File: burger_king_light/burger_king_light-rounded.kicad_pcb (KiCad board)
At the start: 2 copper layers, 102.1 x 58.7 mm, 58 parts, among them U1 TPS55340PWPR, U2 ICM7555CBAZ, U3 IS32LT3178-GRLA3-TR, U4 IS32LT3178-GRLA3-TR, U5 IS32LT3178-GRLA3-TR

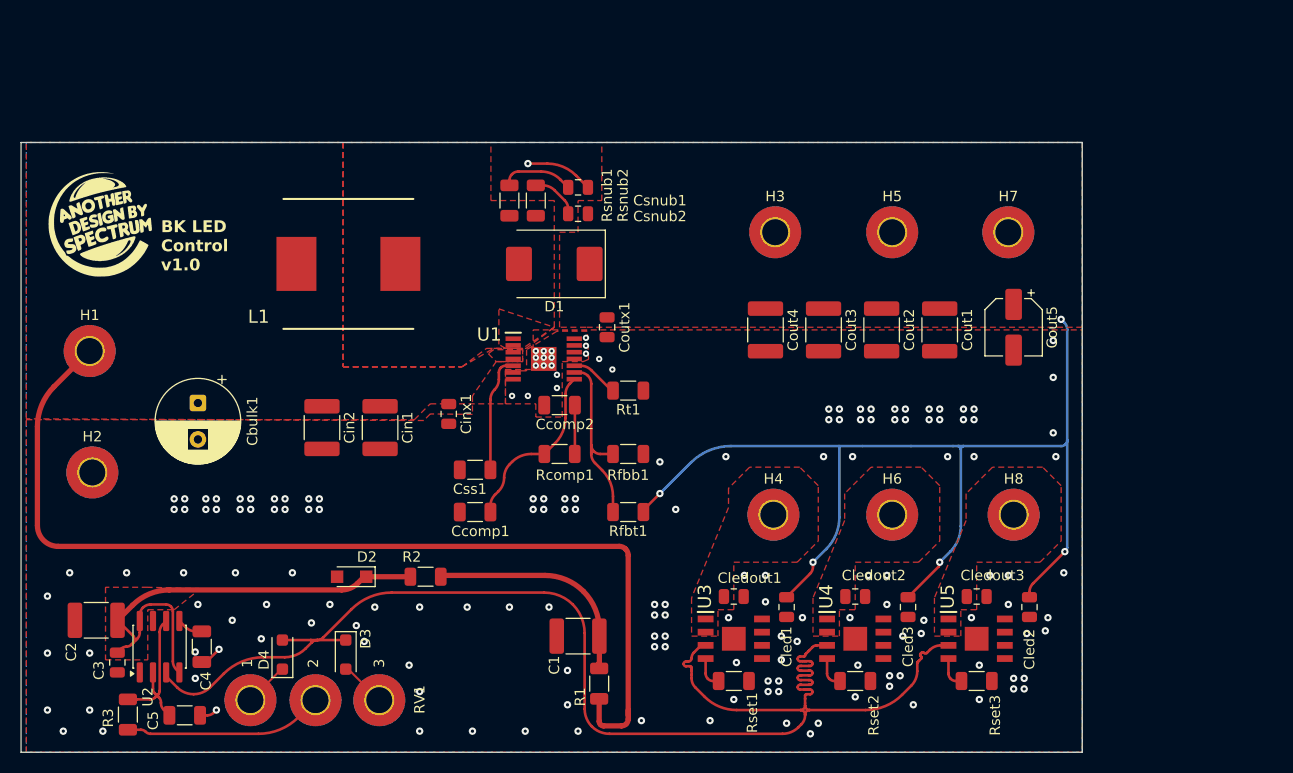
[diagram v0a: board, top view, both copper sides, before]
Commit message: reduced size of board, rerouted connections for LED controllers. rounded tracks. passed DRC, ready for fab, v1.1
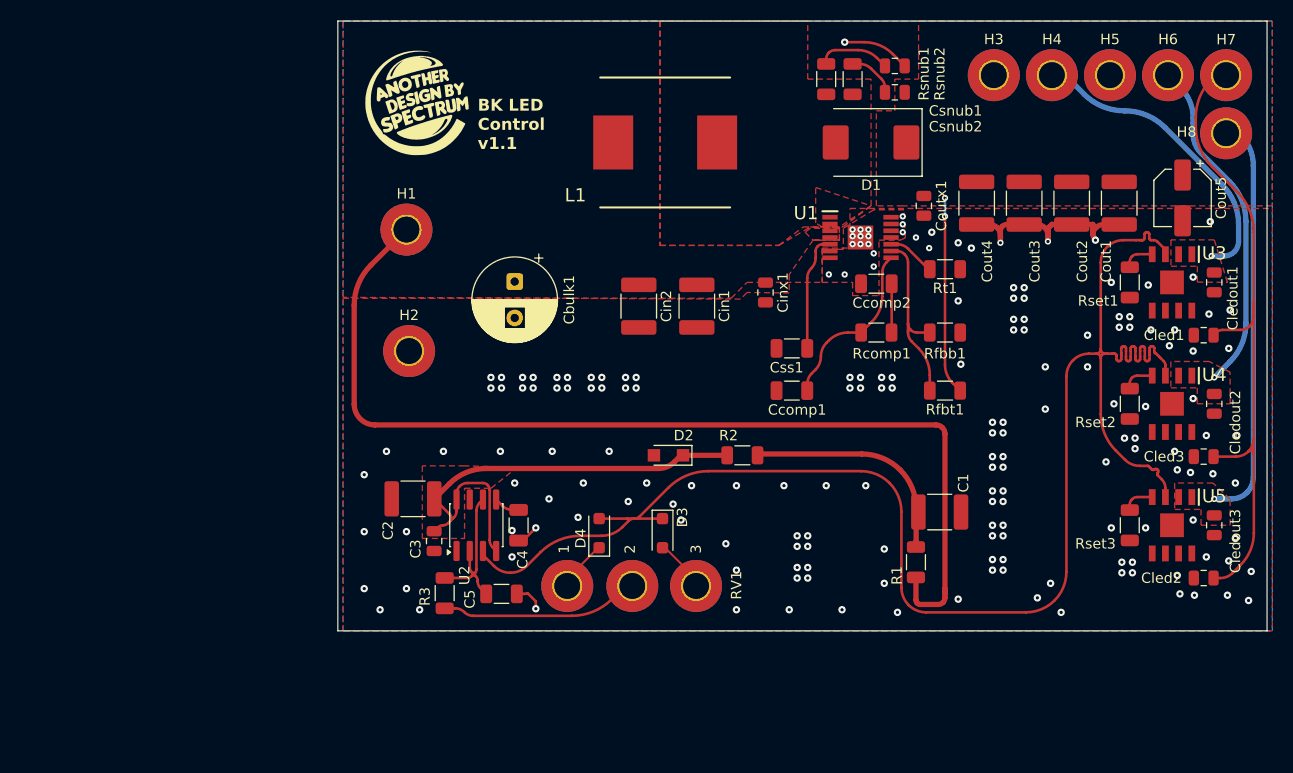
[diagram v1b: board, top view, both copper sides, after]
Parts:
- moved Cledout1 55.2 mm to (182.9, 80.8), turned to -90 degrees
- moved U3 54.3 mm to (178.8, 80.8), turned to -90 degrees
- moved Rset1 54.1 mm to (174.8, 80.8), turned to -90 degrees
- moved H4 50.1 mm to (167.3, 60.8)
- moved H6 49.9 mm to (178.4, 60.8)
- moved Cled1 47.9 mm to (181.9, 85.9), turned to 180 degrees
- moved H8 42.0 mm to (184.0, 66.4)
- moved Cledout2 39.2 mm to (182.9, 92.5), turned to -90 degrees
- moved U4 37.9 mm to (178.8, 92.5), turned to -90 degrees
- moved Rset2 37.5 mm to (174.8, 92.5), turned to -90 degrees
- moved C1 36.8 mm to (156.5, 102.9), turned to 0 degrees
- moved D1 32.6 mm to (149.9, 67.3)
- moved D3 32.6 mm to (129.8, 104.9)
- moved H1 32.6 mm to (105.2, 75.7)
- moved Rt1 32.6 mm to (157.0, 79.5)
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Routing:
- net Net-(U5-OUT_1): track 0.00 -> 40.0 mm, vias 0 -> 1
- net Net-(U4-OUT_1): track 0.00 -> 32.6 mm, vias 0 -> 1
- net Net-(U3-OUT_1): track 0.00 -> 30.0 mm, vias 0 -> 1
- net 0: track 10.4 -> 32.9 mm, vias 169 -> 181
- net +36V: track 105.2 -> 85.2 mm, vias 5 -> 2
- net PWM out: track 137.1 -> 157.1 mm
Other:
- board size 102.1 x 58.7 mm -> 89.4 x 58.7 mm
- board text added: "BK LED Control v1.1"
- board text removed: "BK LED Control v1.0"
